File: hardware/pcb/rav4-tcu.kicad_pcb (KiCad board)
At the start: 2 copper layers, 200 x 150 mm, 140 parts, among them J1 PWR, J2 SOL, J3 SIG, J4 LOAD, K1 G2RL-2 12 V, K2 G2RL-2 12 V, K3 G2RL-2 12 V, Q1 IRF4905, Q2 IRF4905, Q3 IRF4905, U1 ULN2803A, U2 LM393, U3 R-78HB5.0-0.5, X4 DASH, X5 SCREEN, X6 ATF, X7 SHIFT

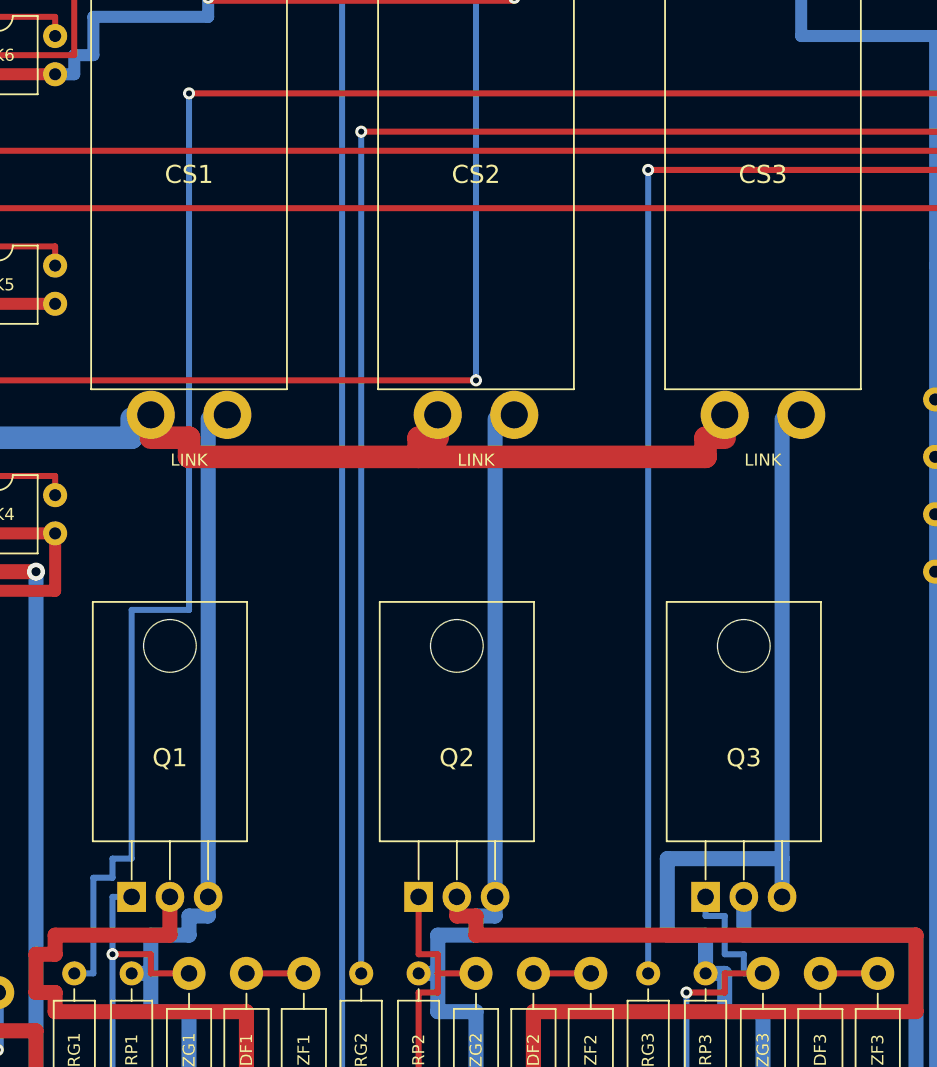
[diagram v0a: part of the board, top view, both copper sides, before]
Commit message: Circuit board: no copper under the bolted MOSFET tabs; posts 2.5 mm taller
Found on review:
- Each IRF4905 lies flat with its metal tab (the drain, switched +12 V) bolted
  to the board, over the ground fill, with only solder mask in between. Now
  there is no copper under the tab on top or around the bolt on either side.
- The board's posts left out the 2.5 mm plastic strip of the male headers that
  sits on the Mega's sockets: 16.1 mm became 18.6 mm. Fit check passes.
- Build book: header strips go in long ends down.
- system_check covers both.

Co-Authored-By: Claude Opus 5.5 <noreply@anthropic.com>
Claude-Session: https://claude.ai/code/session_01ETJrLv4Z1USdoRELecEc2N
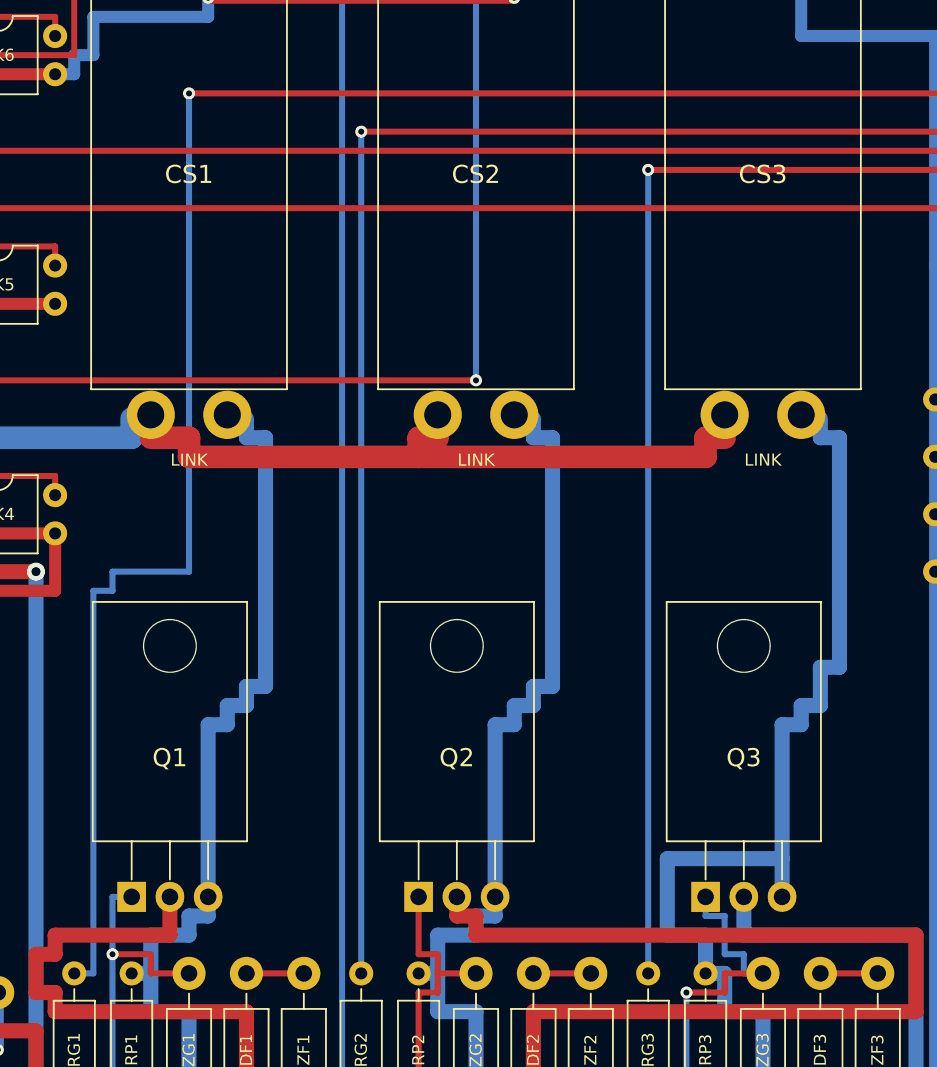
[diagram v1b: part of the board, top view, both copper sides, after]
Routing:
- net SRC3: track 64.0 -> 69.1 mm
- net SRC2: track 55.1 -> 60.2 mm
- net SRC1: track 55.1 -> 60.2 mm

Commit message: Part fit check: every real part at its largest size, against the board
tools/part_fit.py (run by tools/pcb.py, report in hardware/pcb/part_fit.md)
checks each part on the shopping list, at its datasheet maximum or the
biggest version sellers list: legs vs holes, room to bend the legs, bodies vs
neighbours, screw heads, board edge and notch, clearance over the Mega, and
heights for the box's fit check. It found, and the board now fixes:

- square header pins (Mega, modules) had 0.09 mm in 1.0 mm holes: now 1.1 mm
- TO-220 legs (up to 1.03 mm across) in 1.1 mm holes: now 1.3 mm
- a 10 mm-wide 100 uF capacitor would hit the regulator: regulator moved 1.27 mm
- a 33 mm ACS712 module would cover its LINK holes: holes now 35 mm out

Shopping list names the sizes that fit; build book: dry-fit each step,
modules whose pins point up, legs trimmed to 1.5 mm. system_check requires a
clean part fit report.

Co-Authored-By: Claude Opus 5.5 <noreply@anthropic.com>
Claude-Session: https://claude.ai/code/session_01ETJrLv4Z1USdoRELecEc2N
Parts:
- moved U3 1.27 mm to (151.6, 156.8)
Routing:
- net SRC3: track 69.1 -> 65.9 mm
- net SRC2: track 60.2 -> 57.0 mm
- net SRC1: track 60.2 -> 57.0 mm
- net A4: track 110.5 -> 108.0 mm
- net +12_LOG: track 72.8 -> 70.3 mm
- net A5: track 124.5 -> 127.0 mm
- net +12_DRV: track 197.5 -> 195.6 mm
- net LOG: track 45.7 -> 47.0 mm
- net GND: track 1227.5 -> 1228.8 mm, vias 15 -> 13

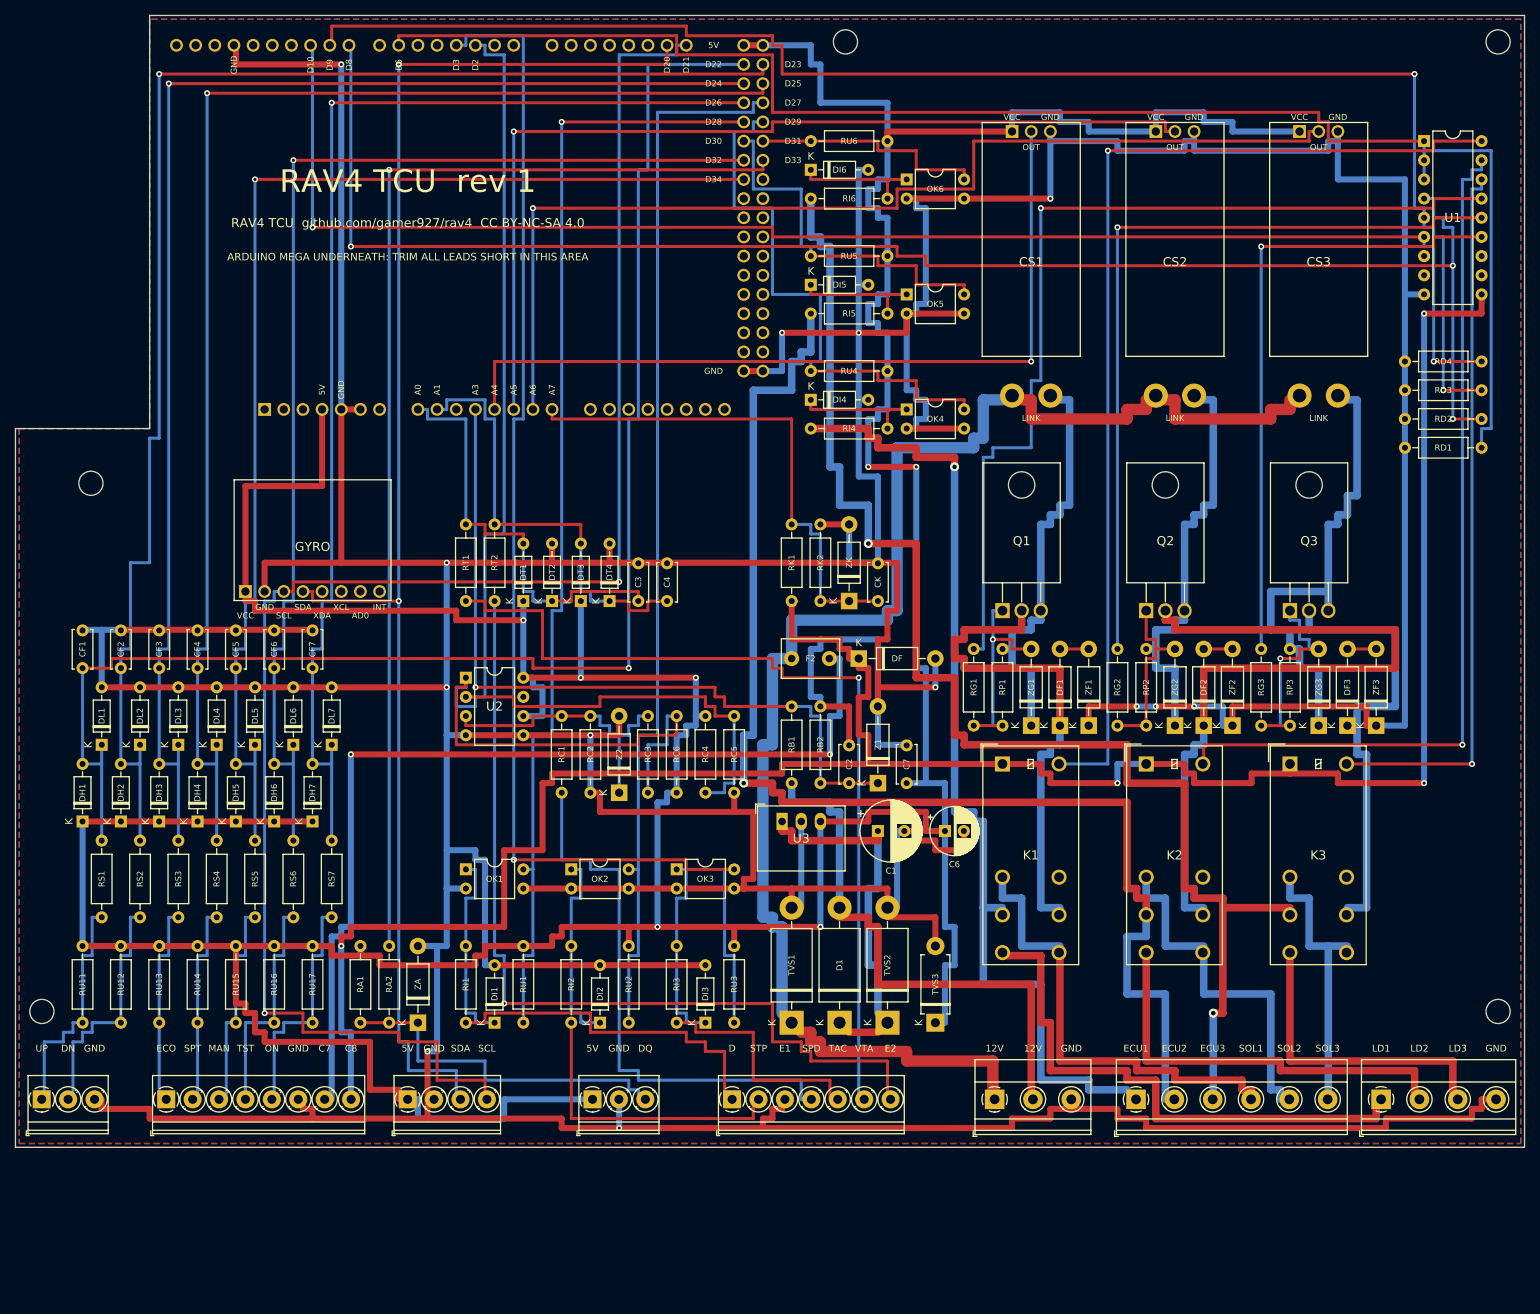
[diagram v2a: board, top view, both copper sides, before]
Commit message: Circuit board rev 2: easier to solder
- 20 mm deeper (200 x 170 mm), the front half spread out; the box grows to
  216 x 212 mm and its fit check passes
- every part's value printed beside its name (RU11 2.2k, DL1 BAT85, ...),
  beside thin parts where it won't fit on them, sized to the room there
- bigger pads: a 0.6 mm copper ring where there's room, long ovals on the chips
- no ground pad joined solidly to the ground fill (hard to heat)
- 5 mm spacing in the crowded rows; sockets for U1 and U2
- router: a wide track leaving a via is now checked at its own width
  (KiCad's DRC caught one too close)

DRC 0 errors / 0 unconnected; part fit 0 problems; make check passes.

Co-Authored-By: Claude Opus 5.5 <noreply@anthropic.com>
Claude-Session: https://claude.ai/code/session_01ETJrLv4Z1USdoRELecEc2N
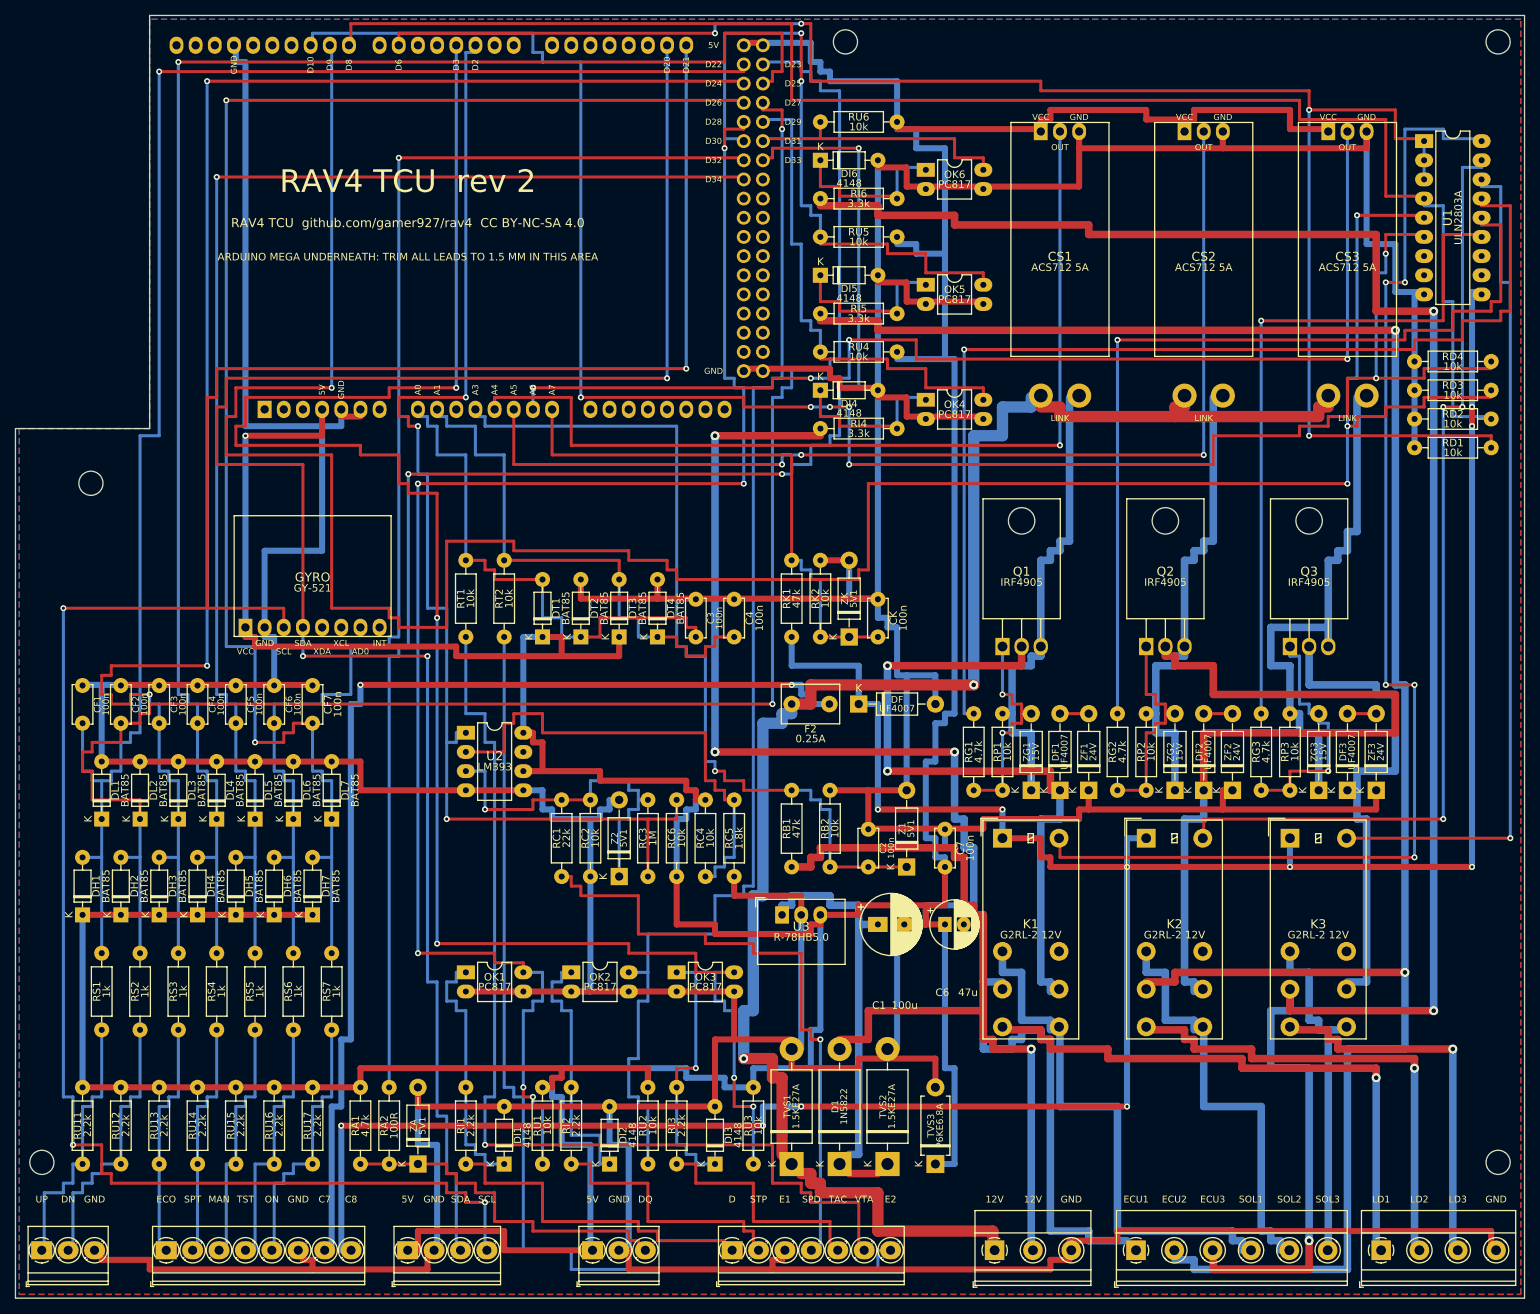
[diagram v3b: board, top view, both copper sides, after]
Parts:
- C1: value 100 µF 50 V -> 100u
- C2, C3, C4, C7, CF1, CF2, CF3, CF4, CF5, CF6, CF7, CK: value 100 nF -> 100n
- C6: value 47 µF 16 V -> 47u
- CS1, CS2, CS3: value ACS712-05B -> ACS712 5A
- DI1, DI2, DI3, DI4, DI5, DI6: value 1N4148 -> 4148
- F2: value PTC 0.25 A -> 0.25A
- K1, K2, K3: value G2RL-2 12 V -> G2RL-2 12V
- OK1, OK2, OK3, OK4, OK5, OK6: footprint DIP-4_W7.62mm -> DIP-4_W7.62mm_LongPads
- RA2: value 100 -> 100R
- U1: footprint DIP-18_W7.62mm -> DIP-18_W7.62mm_LongPads
- U2: footprint DIP-8_W7.62mm -> DIP-8_W7.62mm_LongPads
- U3: value R-78HB5.0-0.5 -> R-78HB5.0
- Z1, Z2, ZA, ZK: value 1N4733A 5.1 V -> 5V1
- ZF1, ZF2, ZF3: value 1N4749A 24 V -> 24V
- ZG1, ZG2, ZG3: value 1N4744A 15 V -> 15V
- moved H1 20.0 mm to (53.5, 202.0)
- moved H2 20.0 mm to (246.5, 202.0)
- moved J1 20.0 mm to (179.8, 213.7)
- moved J2 20.0 mm to (198.5, 213.7)
- moved J3 20.0 mm to (145.0, 213.7)
- moved J4 20.0 mm to (231.0, 213.7)
- moved X4 20.0 mm to (70.0, 213.7)
- moved X5 20.0 mm to (102.0, 213.7)
- moved X6 20.0 mm to (126.5, 213.7)
- moved X7 20.0 mm to (53.5, 213.7)
- moved RU1 18.9 mm to (119.8, 202.2)
- moved RU2 18.9 mm to (133.8, 202.2)
- moved RU3 18.9 mm to (147.8, 202.2)
- moved DI1 18.8 mm to (114.8, 202.2)
- moved DI2 18.8 mm to (128.7, 202.2)
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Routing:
- net D9: track 203.7 -> 338.6 mm, vias 2 -> 4
- net GND: track 1228.8 -> 1119.4 mm, vias 13 -> 0
- net ECU_2: track 173.5 -> 272.0 mm, vias 1 -> 2
- net D21: track 225.3 -> 311.0 mm, vias 2 -> 4
- net ECU_3: track 183.7 -> 269.4 mm, vias 2 -> 3
- net D3: track 174.0 -> 250.8 mm, vias 1 -> 5
- net D28: track 149.9 -> 208.9 mm, vias 1 -> 6
- net D10: track 197.4 -> 254.8 mm, vias 2 -> 7
- net +12_COIL: track 307.4 -> 363.9 mm, vias 4 -> 11
- net +5V: track 676.4 -> 730.4 mm, vias 7 -> 1
- net D20: track 198.0 -> 252.0 mm, vias 2 -> 3
- net ECU_1: track 132.9 -> 184.3 mm, vias 1 -> 3
- net D33: track 153.7 -> 201.3 mm, vias 1 -> 3
- net D23: track 193.0 -> 239.4 mm
- net D26: track 160.0 -> 203.8 mm, vias 1 -> 2
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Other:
- board size 200 x 150 mm -> 200 x 170 mm
- board text added: "ARDUINO MEGA UNDERNEATH: TRIM ALL LEADS TO 1.5 MM IN THIS AREA"
- board text added: "RAV4 TCU rev 2"
- board text removed: "ARDUINO MEGA UNDERNEATH: TRIM ALL LEADS SHORT IN THIS AREA"
- board text removed: "RAV4 TCU rev 1"
